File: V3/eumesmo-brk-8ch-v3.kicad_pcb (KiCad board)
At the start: 2 copper layers, 105 x 67.8 mm, 16 parts, among them J1 Jack RJ45, J10 250-206, J11 250-206, J12 250-206, J13 250-206, J2 Jack RJ45, J3 Jack RJ45, J4 Jack RJ45, J5 Jack RJ45, J6 Jack RJ45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

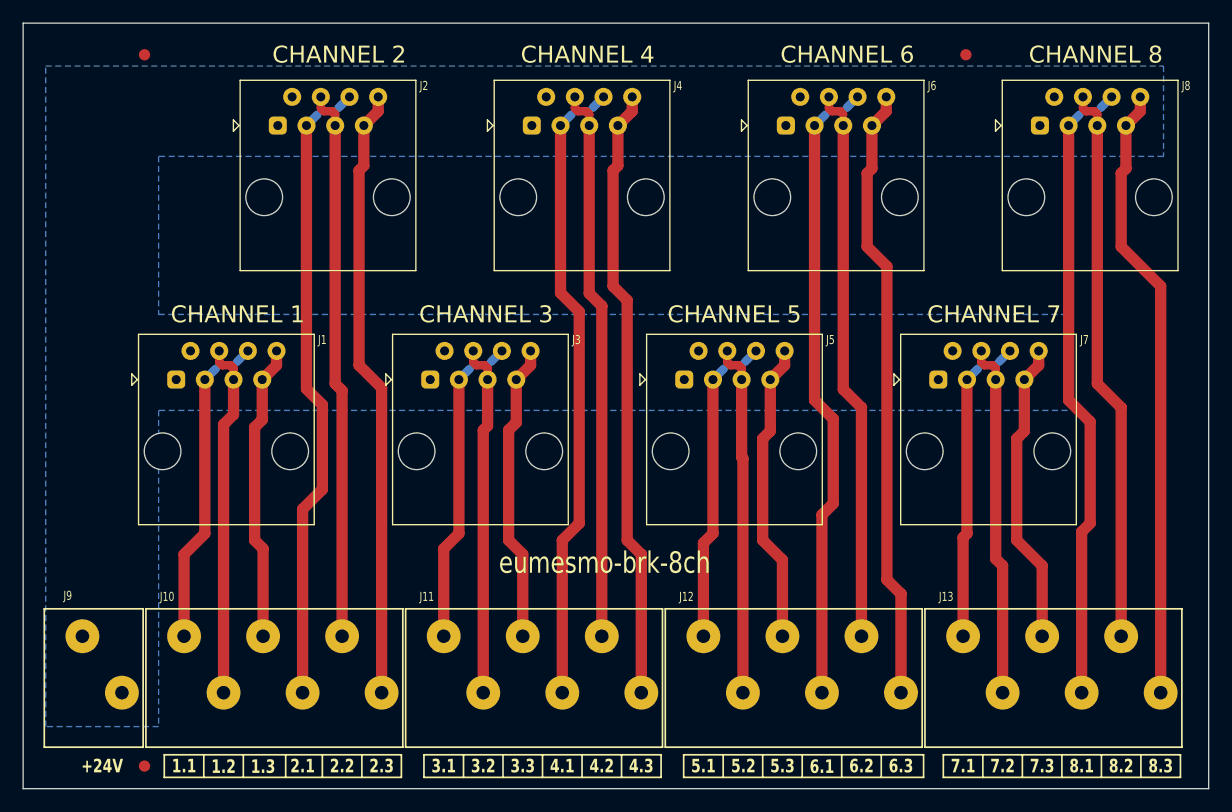
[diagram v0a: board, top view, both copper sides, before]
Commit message: Renamed all files to the eumesmo branding.
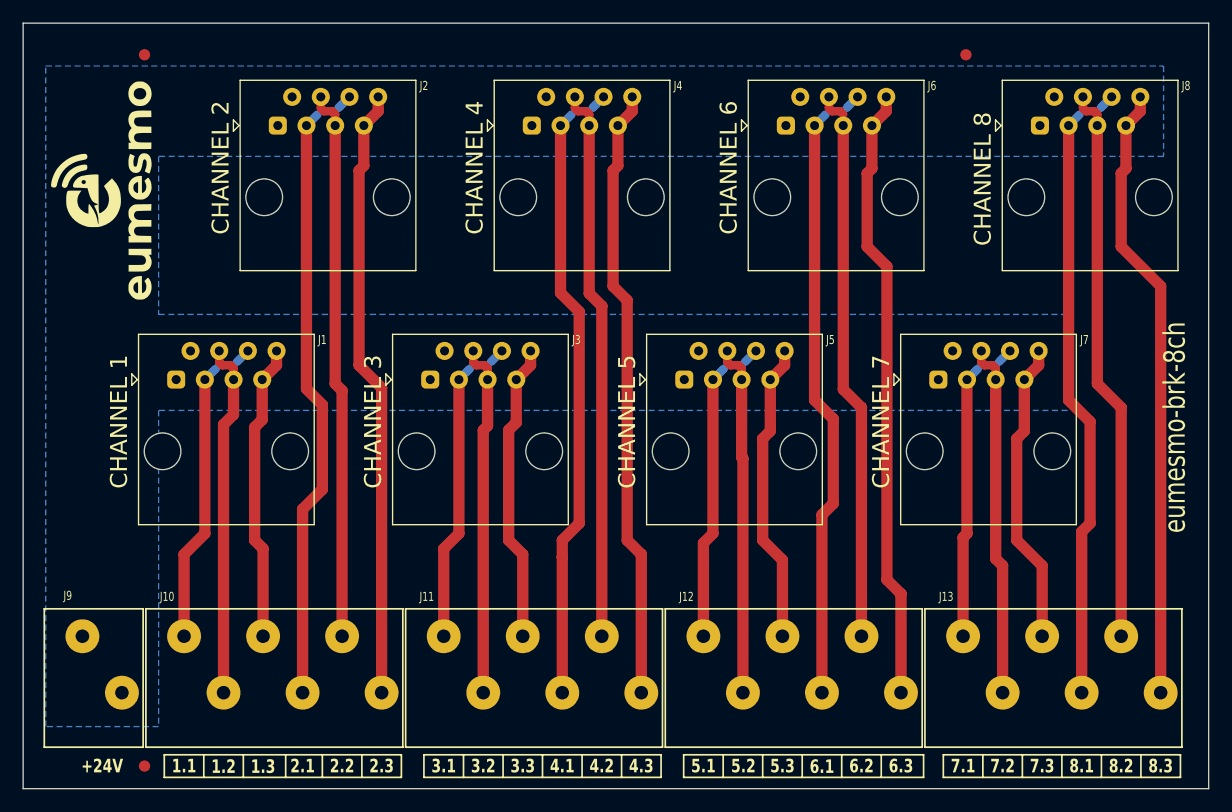
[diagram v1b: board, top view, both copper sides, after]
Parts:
- added G***: LOGO, Tales:Eumesmo_medium_silk, F.Cu at (107.0, 77.0)

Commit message: Added revision date to silkscreen.
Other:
- board text added: "V3.1 2026-06-16"
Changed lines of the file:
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@@
+		(layer "F.SilkS")
+	)
+	(gr_rect
+		(start 197 93.25)
+		(end 198.75 103.75)
+		(stroke
+			(width 0.1)
+			(type default)
+		)
+		(fill no)
 		(layer "F.SilkS")
 	)
@@
 		(layer "Edge.Cuts")
 	)
+	(gr_text "V3.1 2026-06-16"
+		(at 197.875 98.5 90)
+		(layer "F.SilkS")
+		(effects
+			(font
+				(size 1 0.7)
+				(thickness 0.1)
+			)
+		)
+	)
 	(gr_text "+24V"

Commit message: Release V3.1.0
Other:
- board text added: "V3.1 2026-06-17"
- board text removed: "V3.1 2026-06-16"
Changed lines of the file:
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@@
 	(title_block
 		(title "eumesmo 8 Channel RJ45 Breakout Board")
-		(date "2026-06-13")
+		(date "2026-06-17")
 		(rev "V3.1")
 	)
@@
 		(layer "Edge.Cuts")
 	)
-	(gr_text "V3.1 2026-06-16"
+	(gr_text "V3.1 2026-06-17"
 		(at 197.875 98.5 90)
 		(layer "F.SilkS")
